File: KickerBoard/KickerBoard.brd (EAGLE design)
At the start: 75 x 50 mm, 113 parts, among them J1 53375-0610, Q1 TK12P60W, Q4 BSS138, Q5 BSP130, Q6 ZXTN08400BFF, U1 LPC1549JBD48, U10 AD8601, U11 ADCMP350YKSZ, U2 LM5160QPWPRQ1, U3 UCC27212DPRT, U4 UCC27512DRSR, U5 IC-AD_ADR5041, U6 MCP1700T-33, U7 LT6108-2, U8 UCC27524DGN-NOPAD, U9 INA213

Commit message: 電源監視部分のLPF遮断周波数を下げた
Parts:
- C13: value 1n -> 1u
- R9: value 1k -> 2.4k
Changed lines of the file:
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@@
 <element name="D2" library="Diode" package="SOD523" value="" x="69.85" y="9.525" rot="MR0"/>
 <element name="U7" library="ic-LT" package="MSOP8" value="LT6108-2" x="54.61" y="33.655" rot="R180"/>
-<element name="C13" library="Passive" package="1608" value="1n" x="57.15" y="20.32" rot="MR180"/>
-<element name="R9" library="Passive" package="1608" value="1k" x="57.15" y="22.225" rot="MR180"/>
+<element name="C13" library="Passive" package="1608" value="1u" x="57.15" y="20.32" rot="MR180"/>
+<element name="R9" library="Passive" package="1608" value="2.4k" x="57.15" y="22.225" rot="MR180"/>
 <element name="R10" library="Passive" package="1608" value="100k" x="60.325" y="22.225" rot="MR180"/>
 <element name="R11" library="Passive" package="1608" value="3.9k" x="60.325" y="20.32" rot="MR0"/>

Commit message: KickerBoardの部品表作成(途中)
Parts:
- added C1: 0.33n, Passive:1608
- added R50: 10k, Passive:1608
- C10, C9: value 2.2u -> 0.1u
- C11, C12, C3: value 1u -> 0.1u
- C13: value 1u -> 0.22u
- C17: value (none) -> 0.1u
- C5: value 47u -> 22u
- C6, C7: value 22u -> 0.22u
- C8: value 10u -> 4.7u; device Passive:1608 -> Passive:3216
- D9: value (none) -> RB520S
- R11: value 3.9k -> 4.7k
- R29, R31: value 10k -> 33k
- R30: value 1k -> 2.2k
- R4: value 10 -> 100
- R45, R46, R47: value (none) -> 100
- moved C8 1.63 mm to (71.5, 29.2), turned to 90 degrees
- moved C6 0.28 mm to (67.8, 20.1), turned to 0 degrees
- moved C7 0.19 mm to (70.7, 22.2)
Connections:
- net GND: now also C1.2, R50.1
- net N$20: now also R50.2
- net VOLT_CUR: now also C1.1
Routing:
- net GND: track 57.4 -> 69.0 mm, vias 28 -> 26
- net +12V: track 87.5 -> 90.5 mm
- net N$20: track 14.5 -> 16.3 mm
- net N$11: track 16.2 -> 14.5 mm
- net N$10: track 3.68 -> 5.05 mm
- net N$25: track 23.3 -> 24.4 mm
- net VOLT_CUR: track 24.5 -> 25.4 mm, vias 1 -> 2

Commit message: メインとの通信をSPIからCANに切り替えた
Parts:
- added IC1: MAX3051ESA+, MAX3051ESA+:SOIC127P600X175-8N
- added R51: 10k, MotorDriver:R1005
- J1: value 53375-0610 -> SM03B-ZESS-TB; device MotorDriver:53375-0610_53375-0610 -> SM03B-ZESS-TB:SM03B-ZESS-TB
- moved J1 3.81 mm to (69.2, 7.62)
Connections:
- removed net !CS: J1.2, U1.19
- removed net CLK: J1.5, U1.13
- removed net MISO: J1.3, U1.18
- removed net MOSI: J1.4, U1.15
- new net CANH: IC1.7, J1.1
- new net CANL: IC1.6, J1.2
- new net CAN_RX: IC1.4, U1.19
- new net CAN_TX: IC1.1, U1.18
- new net N$34: IC1.5, R51.2
- net +3V3: now also IC1.3
- net +5V: no longer J1.1
- net GND: now also IC1.2, IC1.8, J1.3, R51.1; no longer J1.6
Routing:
- net CAN_TX: track 0.00 -> 13.9 mm, vias 0 -> 1
- net !CS: track 12.9 -> 0.00 mm
- net MISO: track 11.3 -> 0.00 mm
- net CAN_RX: track 0.00 -> 10.3 mm, vias 0 -> 1
- net MOSI: track 9.84 -> 0.00 mm
- net +5V: track 16.0 -> 6.56 mm
- net CLK: track 8.22 -> 0.00 mm
- net +3V3: track 182.0 -> 189.3 mm
- net CANH: track 0.00 -> 6.28 mm, vias 0 -> 1
- net CANL: track 0.00 -> 5.78 mm, vias 0 -> 1
- net N$34: track 0.00 -> 3.14 mm

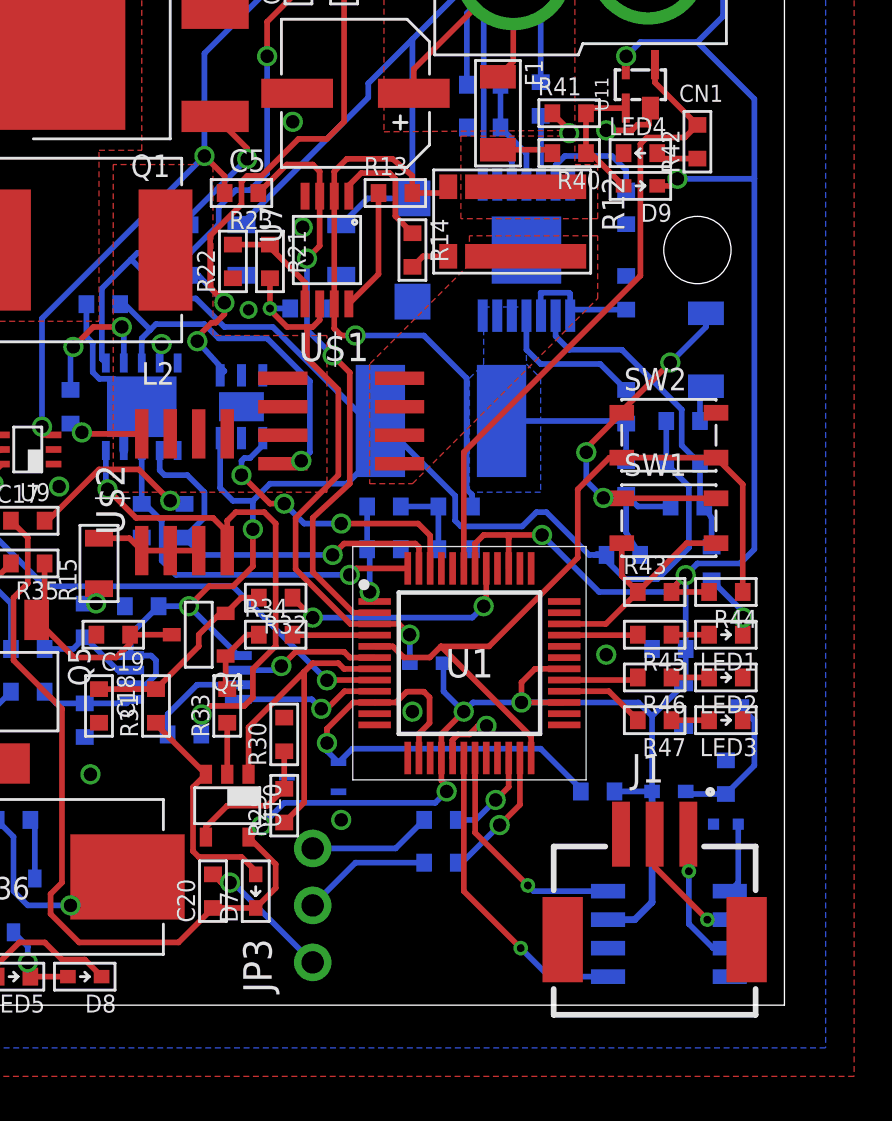
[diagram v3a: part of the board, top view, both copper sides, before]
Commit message: 書き込み部・電源部を変更
*書き込みをUARTからUSBに変更
  *USBコネクタを追加
  *12[MHz]クロックを追加
  *保護ICを追加
  *ピンヘッダを削除
*5[V]電源の削除
  *5[V]を使用している箇所がなかったので無くした
  *レギュレータを5[V]->3.3[V]から12[V]->3.3[V]に
  *USBのVBUSはレギュレータのみに入る
  *VBUS, 12[V]へ逆流防止ダイオードを追加
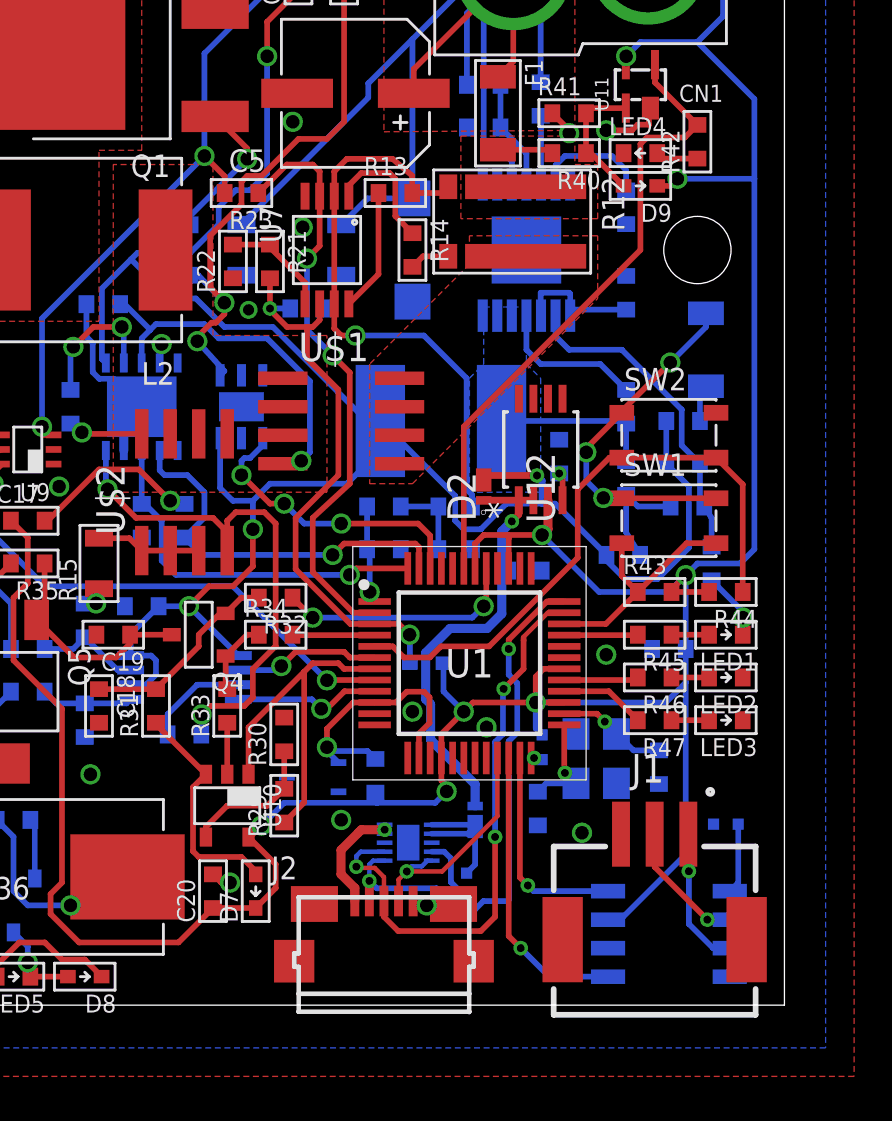
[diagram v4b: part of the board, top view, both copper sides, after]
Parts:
- removed JP3: (no value), MotorDriver:HEADER_1X03_ROUND
- removed U6: MCP1700T-33, MotorDriver:IC-MICROCHIP_SOT23-3
- added C22: 470p, Passive:1608
- added C23, C24: (no value), MotorDriver:C1608
- added D11: SDM2U40CSP-7B, SDM2U40CSP-7B:X3-WLB1608-2
- added IC2: TPD4S014DSQR, TPD4S014DSQR:SON40P200X200X80-11N
- added J2: J_USB_MICROAB_HIROSE_ZX62-AB-5PA, j_usb_hirose_zx62-ab-5pa:J_USB_MICROAB_HIROSE_ZX62-AB-5PA
- added U12: MIC5219-3.3YMM, MIC5219-3.3YMM:MSOP-8_MM
- added Y1: FA238V, FA238V:EPSON_FA238V
- D2: value (none) -> SDM2U40CSP-7B; device Diode:SOD523 -> SDM2U40CSP-7B:X3-WLB1608-2
- R48, R49: value 100 -> 10k; device MotorDriver:R1608 -> MotorDriver:R1005
- moved D2 15.9 mm to (61.6, 23.1), flipped to the top, turned to 90 degrees
- moved C11 12.8 mm to (63.4, 19.4), turned to 180 degrees
- moved R8 9.93 mm to (56.8, 10.2), turned to 270 degrees
- moved R48 6.84 mm to (64.2, 11.5), turned to 270 degrees
- moved R49 3.14 mm to (60.8, 5.33), turned to 90 degrees
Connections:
- removed net N$52: JP3.3, R49.2
- removed net RX: R49.1, U1.22
- removed net TX: R48.1, U1.23
- new net D+: IC2.7, J2.P$3, U1.35
- new net D-: IC2.6, J2.P$2, U1.36
- new net ID: IC2.5, J2.P$4, U1.21
- new net N$40: C11.1, D11.1, D2.1, U12.1, U12.2
- new net N$50: R48.2, U1.24
- new net N$51: IC2.4, R49.1
- new net N$54: C22.1, U12.4
- new net N$56: IC2.10, IC2.9, J2.P$1
- net !ISP: no longer U1.24
- net +12V: now also D2.2
- net +3V3: now also R48.1, U12.3; no longer D2.A, U6.2
- net +5V: now also D11.2, IC2.1, IC2.2, R49.2; no longer C11.1, D2.K, U6.3
- net CAN_RX: now also U1.23; no longer U1.19
- net CAN_TX: now also U1.22; no longer U1.18
- net GND: now also C22.2, C23.2, C24.2, IC2.11, IC2.3, IC2.8, J2.P$5, J2.SHIELD1, J2.SHIELD2, J2.SHIELD3, J2.SHIELD4, U12.5, U12.6, U12.7, U12.8, Y1.2, Y1.4; no longer JP3.1, U6.1
- net N$47: now also C24.1, U1.26, Y1.3; no longer U1.21
- net N$48: now also C23.1, U1.25, Y1.1; no longer JP3.2, R48.2
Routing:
- net D+: track 0.00 -> 25.9 mm, vias 0 -> 3
- net D-: track 0.00 -> 24.6 mm, vias 0 -> 2
- net N$40: track 0.00 -> 19.8 mm, vias 0 -> 1
- net ID: track 0.00 -> 10.4 mm, vias 0 -> 1
- net VREF: track 21.9 -> 12.3 mm
- net GND: track 69.0 -> 61.4 mm, vias 26 -> 28
- net !ISP: track 34.0 -> 27.4 mm
- net TX: track 5.92 -> 0.00 mm, vias 1 -> 0
- net N$52: track 5.49 -> 0.00 mm
- net N$56: track 0.00 -> 5.25 mm, vias 0 -> 1
- net N$47: track 0.00 -> 4.93 mm, vias 0 -> 1
- net RX: track 4.17 -> 0.00 mm, vias 1 -> 0
- net N$51: track 0.00 -> 3.02 mm
- net +12V: track 90.5 -> 93.5 mm, vias 3 -> 4
- net +3V3: track 189.3 -> 191.4 mm
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
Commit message: viaの数とかを調節した
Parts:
- added R52, R53: 2.2, MotorDriver:R1608
- R19: value 10 -> 2.2; device Passive:2012 -> MotorDriver:R1608
- moved R50 2.56 mm to (47.2, 30.9), turned to 90 degrees
- moved R19 0.65 mm to (48.1, 34.3)
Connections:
- new net N$52: R52.2, U$1.4
- new net N$53: R53.2, U$2.4
- net GND: no longer R50.1
- net N$19: now also R53.1; no longer U$2.4
- net N$20: now also R52.1; no longer U$1.4
- net N$21: now also R50.1
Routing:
- net N$20: track 16.3 -> 7.70 mm
- net CHARGE1: track 15.1 -> 20.8 mm, vias 2 -> 7
- net N$52: track 0.00 -> 4.84 mm
- net GND: track 61.4 -> 57.4 mm, vias 28 -> 45
- net N$19: track 24.2 -> 22.5 mm, vias 2 -> 3
- net N$21: track 4.25 -> 4.98 mm
- net N$25: track 24.4 -> 25.1 mm
- net N$53: track 0.00 -> 0.67 mm, vias 0 -> 1
- net GATE_BOOST: track 13.2 -> 12.6 mm

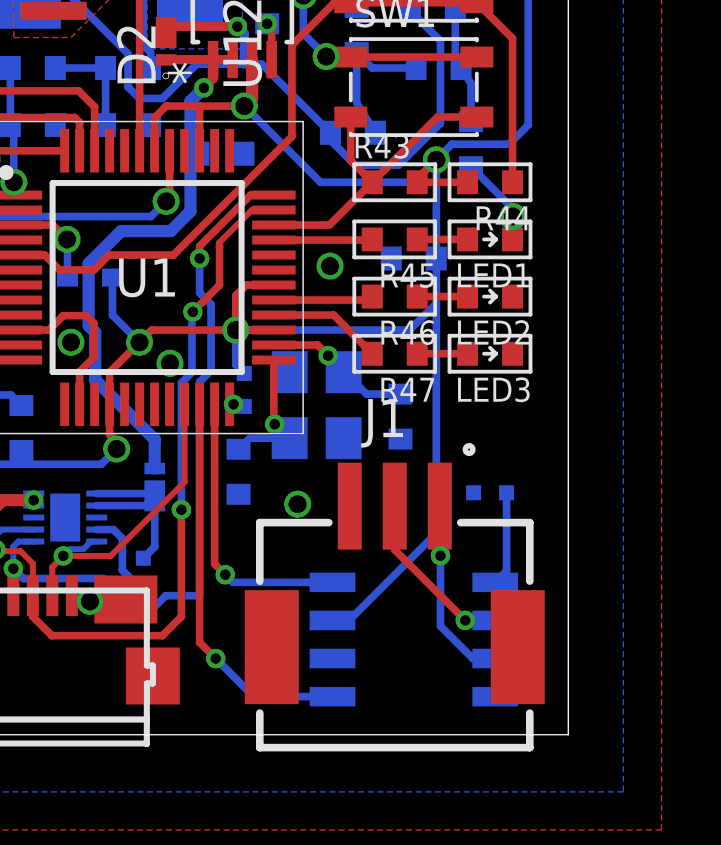
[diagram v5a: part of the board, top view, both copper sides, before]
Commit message: [fix] Kickerのコネクタのアサインを変更
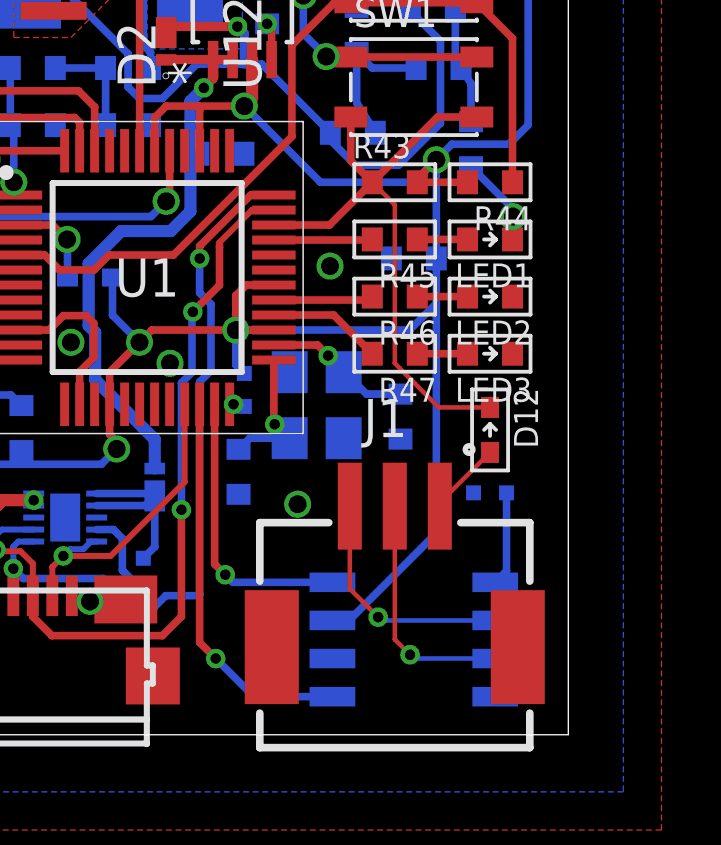
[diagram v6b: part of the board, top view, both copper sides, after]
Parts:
- added D12: (no value), MotorDriver:MOTORDRIVER_DIODE_SOD523
- D1: value SMAJ60 -> SMAJ54A
- F1: value 10 -> 15
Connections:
- removed net CANH: IC1.7, J1.1
- removed net CANL: IC1.6, J1.2
- new net N$55: IC1.6, J1.3
- new net N$57: IC1.7, J1.2
- new net N$58: D12.A, J1.1
- net !RST: now also D12.K
- net GND: no longer J1.3
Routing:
- net !RST: track 10.7 -> 20.9 mm
- net N$57: track 0.00 -> 8.06 mm, vias 0 -> 1
- net N$55: track 0.00 -> 8.04 mm, vias 0 -> 1
- net CANH: track 6.28 -> 0.00 mm, vias 1 -> 0
- net CANL: track 5.78 -> 0.00 mm, vias 1 -> 0
- net N$58: track 0.00 -> 2.48 mm
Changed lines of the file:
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@@
 <?xml version="1.0" encoding="utf-8"?>
 <!DOCTYPE eagle SYSTEM "eagle.dtd">
-<eagle version="8.6.3">
+<eagle version="8.7.1">
 <drawing>
 <settings>
@@
 <element name="C9" library="Passive" package="2012" value="0.1u" x="55.245" y="33.655" rot="MR270"/>
 <element name="C10" library="Passive" package="2012" value="0.1u" x="50.8" y="33.655" rot="MR270"/>
-<element name="F1" library="Passive" package="3216" value="10" x="62.23" y="39.751" rot="R270"/>
+<element name="F1" library="Passive" package="3216" value="15" x="62.23" y="39.751" rot="R270"/>
 <element name="C5" library="Passive" package="ES-6.3" value="22u" x="55.88" y="40.64" rot="R180"/>
-<element name="D1" library="Diode" package="DO-214AC" value="SMAJ60" x="58.42" y="33.655" rot="MR270"/>
+<element name="D1" library="Diode" package="DO-214AC" value="SMAJ54A" x="58.42" y="33.655" rot="MR270"/>
 <element name="C12" library="Passive" package="1608" value="0.1u" x="69.85" y="15.875" rot="MR0"/>
 <element name="U7" library="ic-LT" package="MSOP8" value="LT6108-2" x="54.61" y="33.655" rot="R180"/>
@@
 <element name="R52" library="MotorDriver" library_urn="urn:adsk.eagle:library:1073580" package="R1608" package3d_urn="urn:adsk.eagle:package:1073656/2" value="2.2" x="50.3555" y="28.2575" rot="R270"/>
 <element name="R53" library="MotorDriver" library_urn="urn:adsk.eagle:library:1073580" package="R1608" package3d_urn="urn:adsk.eagle:package:1073656/2" value="2.2" x="51.308" y="20.7645" rot="MR0"/>
+<element name="D12" library="MotorDriver" package="MOTORDRIVER_DIODE_SOD523" value="" x="72.39" y="10.16" rot="R270"/>
 </elements>
 <signals>
@@
 <contactref element="R51" pad="1"/>
 <contactref element="IC1" pad="8"/>
-<contactref element="J1" pad="3"/>
 <contactref element="U12" pad="6"/>
 <contactref element="U12" pad="7"/>
@@
 <wire x1="68.465" y1="18.415" x2="70.64" y2="20.59" width="0.254" layer="1"/>
 <wire x1="70.64" y1="20.59" x2="71.95" y2="20.59" width="0.254" layer="1"/>
+<contactref element="D12" pad="K"/>
+<wire x1="69.3864" y1="12.2053125" x2="69.3864" y2="12.2111" width="0.1524" layer="1"/>
+<wire x1="69.3864" y1="12.2111" x2="69.215" y2="12.3825" width="0.1524" layer="1"/>
+<wire x1="72.39" y1="10.91" x2="70.6817125" y2="10.91" width="0.1524" layer="1"/>
+<wire x1="70.6817125" y1="10.91" x2="69.3864" y2="12.2053125" width="0.1524" layer="1"/>
+<wire x1="69.215" y1="12.3825" x2="69.215" y2="17.665" width="0.1524" layer="1"/>
+<wire x1="69.215" y1="17.665" x2="68.465" y2="18.415" width="0.1524" layer="1"/>
 </signal>
 <signal name="N$70">
@@
 <wire x1="72.94" y1="8.0645" x2="72.94" y2="5.458" width="0.254" layer="16"/>
 <wire x1="72.94" y1="5.458" x2="72.562" y2="5.08" width="0.254" layer="16"/>
-</signal>
-<signal name="CANH">
-<contactref element="IC1" pad="7"/>
-<contactref element="J1" pad="1"/>
-<wire x1="72.562" y1="2.54" x2="71.8185" y2="2.54" width="0.254" layer="16"/>
-<wire x1="71.8185" y1="2.54" x2="70.739" y2="3.6195" width="0.254" layer="16"/>
-<wire x1="70.739" y1="3.6195" x2="70.739" y2="5.969" width="0.254" layer="16"/>
-<via x="70.739" y="5.969" extent="1-16" drill="0.35" shape="octagon"/>
-<wire x1="70.739" y1="5.969" x2="70.739" y2="7.596" width="0.254" layer="1"/>
-<wire x1="70.739" y1="7.596" x2="70.715" y2="7.62" width="0.254" layer="1"/>
-</signal>
-<signal name="CANL">
-<contactref element="IC1" pad="6"/>
-<contactref element="J1" pad="2"/>
-<wire x1="72.562" y1="3.81" x2="71.5645" y2="3.81" width="0.254" layer="16"/>
-<via x="71.5645" y="3.81" extent="1-16" drill="0.35" shape="octagon"/>
-<wire x1="71.5645" y1="3.81" x2="69.215" y2="6.1595" width="0.254" layer="1"/>
-<wire x1="69.215" y1="6.1595" x2="69.215" y2="7.62" width="0.254" layer="1"/>
 </signal>
 <signal name="N$40">
@@
 <wire x1="50.165" y1="20.3715" x2="50.165" y2="20.26" width="0.254" layer="1"/>
 </signal>
+<signal name="N$55">
+<contactref element="IC1" pad="6"/>
+<contactref element="J1" pad="3"/>
+<wire x1="67.715" y1="7.62" x2="67.715" y2="4.86385" width="0.1524" layer="1"/>
+<wire x1="67.715" y1="4.86385" x2="68.659" y2="3.91985" width="0.1524" layer="1"/>
+<via x="68.659" y="3.91985" extent="1-16" drill="0.35" shape="octagon"/>
+<wire x1="68.659" y1="3.91985" x2="68.76885" y2="3.81" width="0.1524" layer="16"/>
+<wire x1="68.76885" y1="3.81" x2="72.562" y2="3.81" width="0.1524" layer="16"/>
+</signal>
+<signal name="N$57">
+<contactref element="IC1" pad="7"/>
+<contactref element="J1" pad="2"/>
+<wire x1="69.215" y1="7.62" x2="69.215" y2="3.175" width="0.1524" layer="1"/>
+<via x="69.723" y="2.667" extent="1-16" drill="0.35" shape="octagon"/>
+<wire x1="69.723" y1="2.667" x2="69.85" y2="2.54" width="0.1524" layer="16"/>
+<wire x1="69.85" y1="2.54" x2="72.562" y2="2.54" width="0.1524" layer="16"/>
+<wire x1="69.215" y1="3.175" x2="69.723" y2="2.667" width="0.1524" layer="1"/>
+</signal>
+<signal name="N$58">
+<contactref element="J1" pad="1"/>
+<contactref element="D12" pad="A"/>
+<wire x1="72.39" y1="9.41" x2="70.715" y2="7.735" width="0.1524" layer="1"/>
+<wire x1="70.715" y1="7.735" x2="70.715" y2="7.62" width="0.1524" layer="1"/>
+</signal>
 </signals>
